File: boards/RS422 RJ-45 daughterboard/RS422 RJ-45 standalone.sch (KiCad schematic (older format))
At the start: 13 parts, among them J201 DB9, J202 DB9, U201 ISL83387E, U202 24AA014

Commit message: Done RS422/485 Daughterboard
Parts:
- removed J202: DB9, symbol DB9
- added J202: RJ45, symbol RJ45
- added P201: CONN_4, symbol CONN_4
- added SW201: DPDT, ~, symbol DPDT_SLIDE-SWITCH
- added U203: ISL8491E, ~, symbol ISL8491E
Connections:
- net labels removed: C_CTS, C_DSR, C_DTR, C_RTS, C_RX, C_TX
- wire segments 90 -> 112
- no-connect marks 4 -> 7
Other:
- moved on the sheet: D201, J201, R201, R203, U201, U202

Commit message: Update RS422 RJ-45 dboard to use RS232 adapter common block
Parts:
- removed C201, C202, C203, C204, C205, C206: 0.1u, ~, symbol CSMALL
- removed D201: LED, ~, symbol LED
- removed J201: DB9, symbol DB9
- removed R201: R, ~, symbol R
- removed U201: ISL83387E, ~, symbol ISL83387E
- added J201: RJ45, symbol RJ45
- added P202: CONN_4X2, symbol CONN_4X2
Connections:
- net labels removed: A_CTS, A_DSR, A_DTR, A_RTS, A_RX, A_TX, B_CTS, B_DSR, B_DTR, B_RTS, B_RX, B_TX
- wire segments 112 -> 72
- no-connect marks 7 -> 10
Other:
- moved on the sheet: J202, P201, SW201, U203

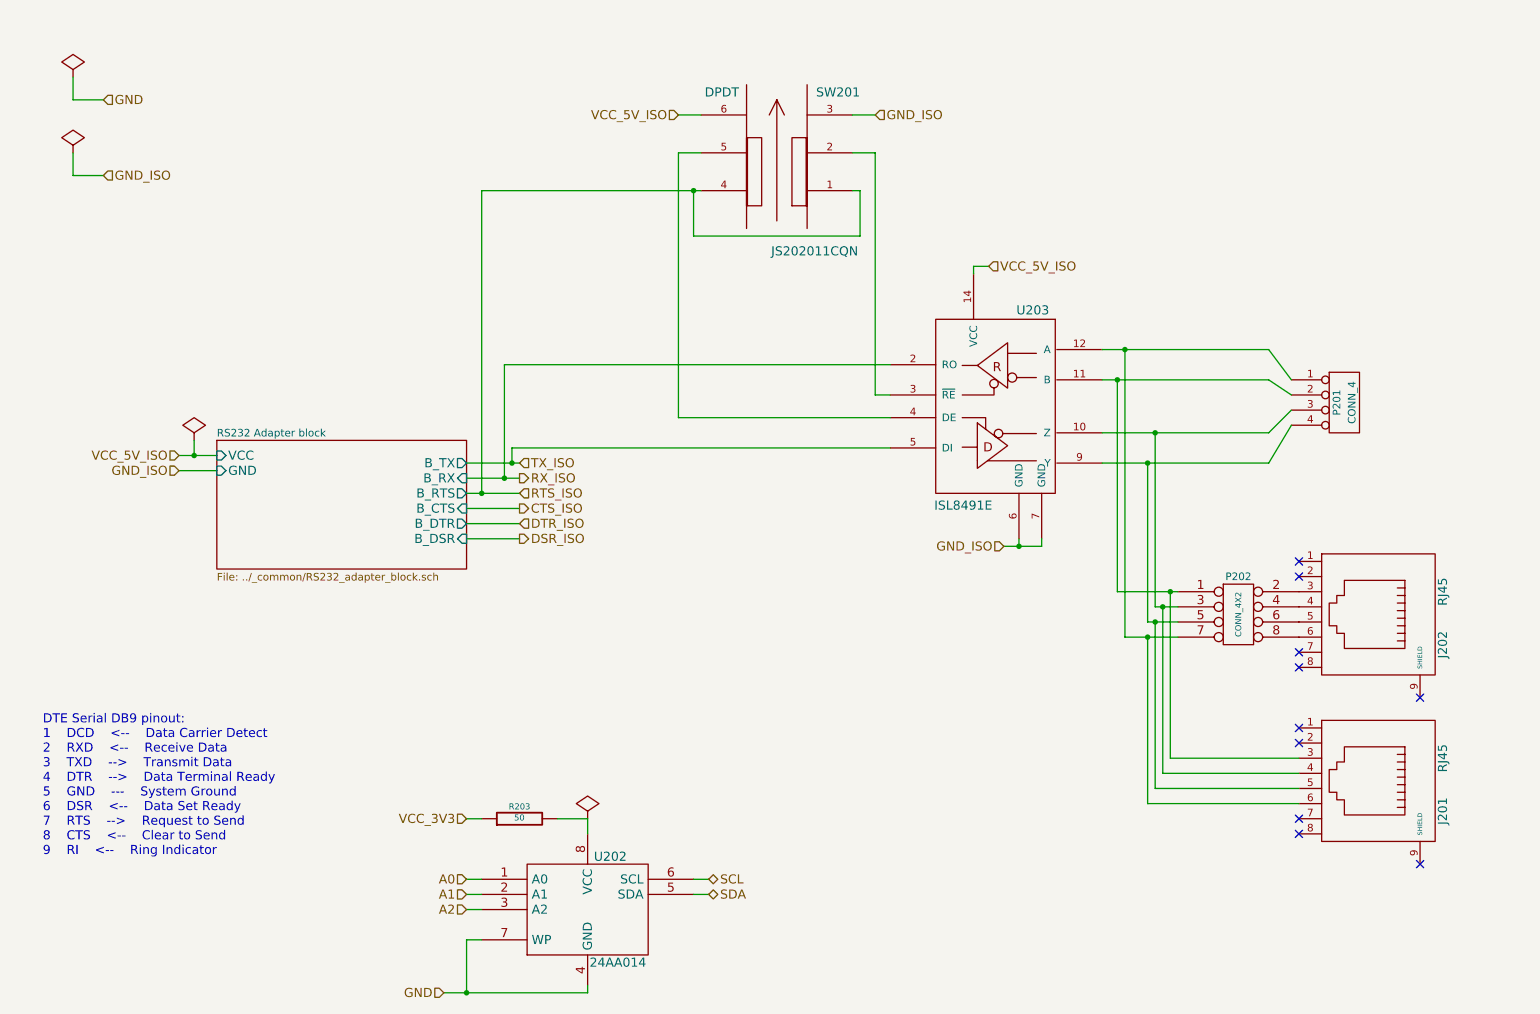
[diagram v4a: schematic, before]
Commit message: Updated RS232 adapter block to include DC jack, changed power pins to passive; Changed power pins on RS422 dboard sheet to passive
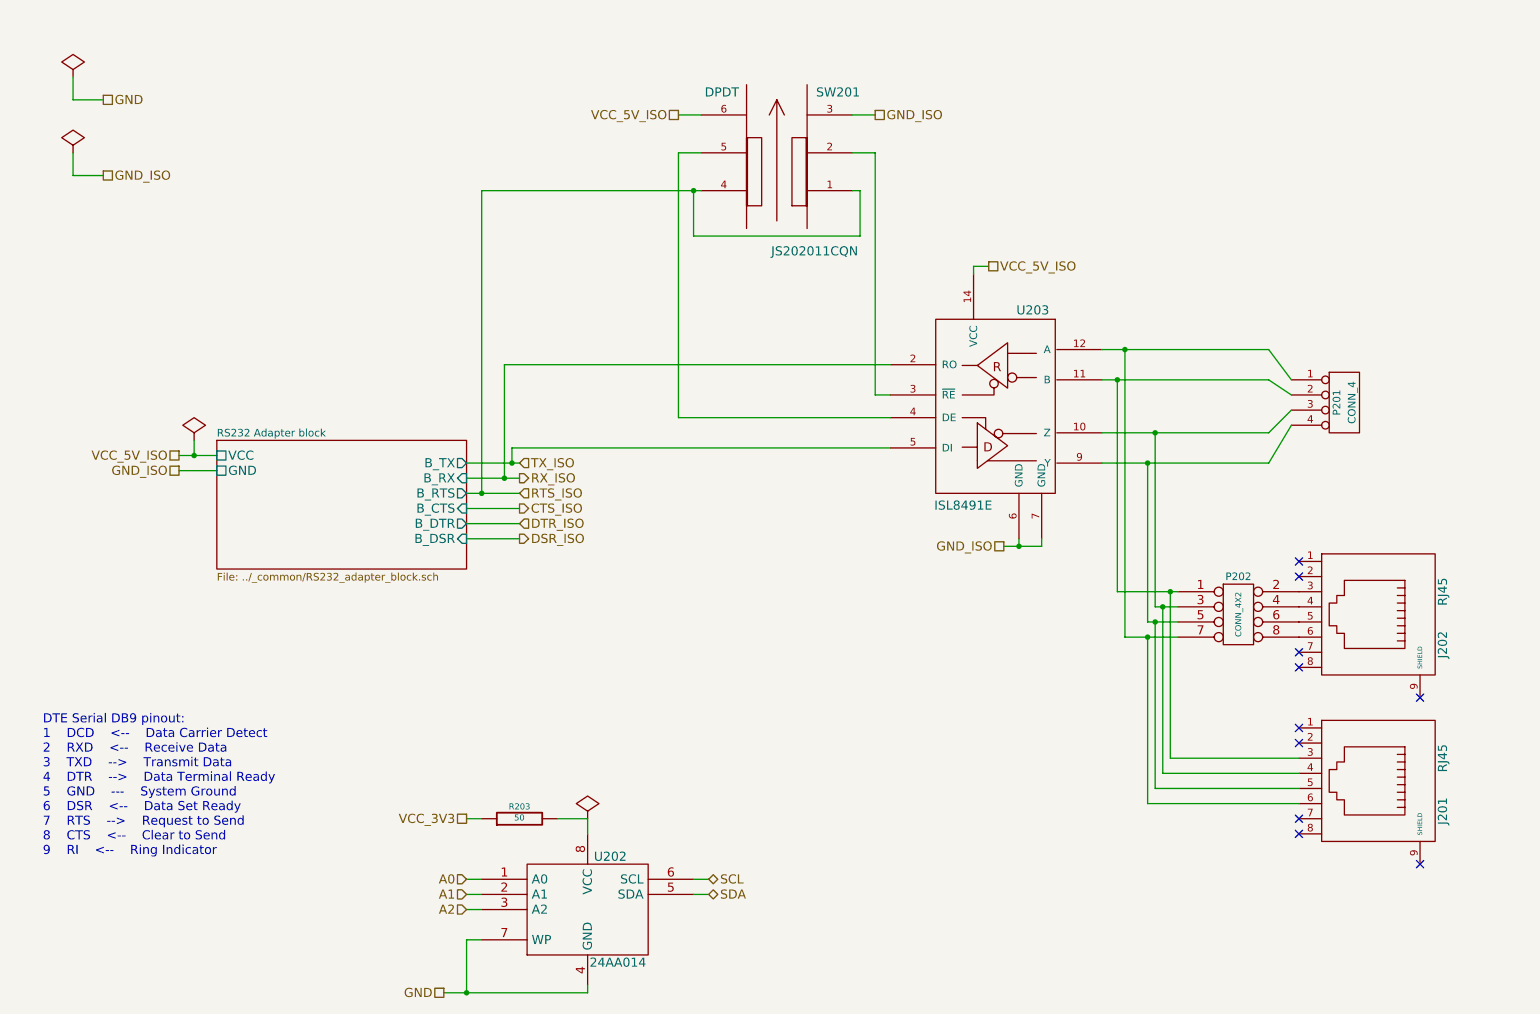
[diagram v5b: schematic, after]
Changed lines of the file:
@@
 Text HLabel 4200 4350 2    60   Output ~ 0
 DSR_ISO
-Text HLabel 3850 6200 0    60   Input ~ 0
+Text HLabel 3850 6200 0    60   UnSpc ~ 0
 VCC_3V3
-Text HLabel 3700 7350 0    60   Input ~ 0
+Text HLabel 3700 7350 0    60   UnSpc ~ 0
 GND
 Text HLabel 5450 6700 2    60   BiDi ~ 0
@@
 	1    0    0    -1
 $EndComp
-Text HLabel 1950 3800 0    60   Input ~ 0
+Text HLabel 1950 3800 0    60   UnSpc ~ 0
 VCC_5V_ISO
-Text HLabel 1950 3900 0    60   Input ~ 0
+Text HLabel 1950 3900 0    60   UnSpc ~ 0
 GND_ISO
 Text Notes 1050 6450 0    60   ~ 0
 DTE Serial DB9 pinout:\n1	DCD	<--	Data Carrier Detect\n2	RXD	<--	Receive Data\n3	TXD	-->	Transmit Data\n4	DTR	-->	Data Terminal Ready\n5	GND	---	System Ground\n6	DSR	<--	Data Set Ready\n7	RTS	-->	Request to Send\n8	CTS	<--	Clear to Send\n9	RI	<--	Ring Indicator
 $Comp
-L PWR_FLAG #FLG01
+L PWR_FLAG #FLG203
 U 1 1 53ABE834
 P 2050 3700
-F 0 "#FLG01" H 2050 3795 30  0001 C CNN
+F 0 "#FLG203" H 2050 3795 30  0001 C CNN
 F 1 "PWR_FLAG" H 2050 3880 30  0001 C CNN
 F 2 "" H 2050 3700 60  0000 C CNN
@@
 $EndComp
 $Comp
-L PWR_FLAG #FLG02
+L PWR_FLAG #FLG204
 U 1 1 53ABE907
 P 4650 6200
-F 0 "#FLG02" H 4650 6295 30  0001 C CNN
+F 0 "#FLG204" H 4650 6295 30  0001 C CNN
 F 1 "PWR_FLAG" H 4650 6380 30  0001 C CNN
 F 2 "" H 4650 6200 60  0000 C CNN
@@
 $EndComp
 $Comp
-L PWR_FLAG #FLG03
+L PWR_FLAG #FLG201
 U 1 1 53ABE910
 P 1250 1300
-F 0 "#FLG03" H 1250 1395 30  0001 C CNN
+F 0 "#FLG201" H 1250 1395 30  0001 C CNN
 F 1 "PWR_FLAG" H 1250 1480 30  0001 C CNN
 F 2 "" H 1250 1300 60  0000 C CNN
@@
 $EndComp
 $Comp
-L PWR_FLAG #FLG04
+L PWR_FLAG #FLG202
 U 1 1 53ABE916
 P 1250 1800
-F 0 "#FLG04" H 1250 1895 30  0001 C CNN
+F 0 "#FLG202" H 1250 1895 30  0001 C CNN
 F 1 "PWR_FLAG" H 1250 1980 30  0001 C CNN
 F 2 "" H 1250 1800 60  0000 C CNN
@@
 	1    0    0    -1
 $EndComp
-Text HLabel 1450 1450 2    60   Input ~ 0
+Text HLabel 1450 1450 2    60   UnSpc ~ 0
 GND
-Text HLabel 1450 1950 2    60   Input ~ 0
+Text HLabel 1450 1950 2    60   UnSpc ~ 0
 GND_ISO
 $Comp
@@
 	0    1    1    0
 $EndComp
-Text HLabel 7300 2550 2    60   Input ~ 0
+Text HLabel 7300 2550 2    60   UnSpc ~ 0
 VCC_5V_ISO
-Text HLabel 7400 4400 0    60   Input ~ 0
+Text HLabel 7400 4400 0    60   UnSpc ~ 0
 GND_ISO
 $Comp
@@
 	0    -1   -1   0
 $EndComp
-Text HLabel 5250 1550 0    60   Input ~ 0
+Text HLabel 5250 1550 0    60   UnSpc ~ 0
 VCC_5V_ISO
-Text HLabel 6550 1550 2    60   Input ~ 0
+Text HLabel 6550 1550 2    60   UnSpc ~ 0
 GND_ISO
 Wire Wire Line
@@
 F0 "RS232 Adapter block" 50
 F1 "../_common/RS232_adapter_block.sch" 50
-F2 "GND" I L 2200 3900 60
-F3 "VCC" I L 2200 3800 60
+F2 "GND" U L 2200 3900 60
+F3 "VCC" U L 2200 3800 60
 F4 "B_RX" I R 3850 3950 60
 F5 "B_TX" O R 3850 3850 60

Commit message: Added bypass capacitor to EEPROM in RS422 dboard
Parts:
- added C201: 0.1u, ~, symbol CSMALL
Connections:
- wire segments 72 -> 75
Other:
- note removed: "DTE Serial DB9 pinout:\n1 DCD <-- Data Carrier Detect\n2 RXD <-- Receive Data\n3 TXD --> Transmit Data\n4 DTR --> Data Terminal Ready\n5 GND --- System Ground\n6 DSR <-- Data Set Ready\n7 RTS --> Request to Send\n8 CTS <-- Clear to Send\n9 RI <-- Ring Indicator"
- moved on the sheet: R203
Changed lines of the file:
@@
 Sheet 2 3
 Title ""
-Date "2 jul 2014"
+Date "3 jul 2014"
 Rev ""
 Comp ""
@@
 Text HLabel 4200 4350 2    60   Output ~ 0
 DSR_ISO
-Text HLabel 3850 6200 0    60   UnSpc ~ 0
+Text HLabel 3350 6200 0    60   UnSpc ~ 0
 VCC_3V3
 Text HLabel 3700 7350 0    60   UnSpc ~ 0
@@
 Text HLabel 1950 3900 0    60   UnSpc ~ 0
 GND_ISO
-Text Notes 1050 6450 0    60   ~ 0
-DTE Serial DB9 pinout:\n1	DCD	<--	Data Carrier Detect\n2	RXD	<--	Receive Data\n3	TXD	-->	Transmit Data\n4	DTR	-->	Data Terminal Ready\n5	GND	---	System Ground\n6	DSR	<--	Data Set Ready\n7	RTS	-->	Request to Send\n8	CTS	<--	Clear to Send\n9	RI	<--	Ring Indicator
 $Comp
 L PWR_FLAG #FLG203
@@
 L R R203
 U 1 1 53ABAC25
-P 4200 6200
-F 0 "R203" V 4280 6200 40  0000 C CNN
-F 1 "50" V 4207 6201 40  0000 C CNN
-F 2 "~" V 4130 6200 30  0000 C CNN
-F 3 "~" H 4200 6200 30  0000 C CNN
-	1    4200 6200
+P 3700 6200
+F 0 "R203" V 3780 6200 40  0000 C CNN
+F 1 "50" V 3707 6201 40  0000 C CNN
+F 2 "~" V 3630 6200 30  0000 C CNN
+F 3 "~" H 3700 6200 30  0000 C CNN
+	1    3700 6200
 	0    -1   -1   0
 $EndComp
@@
 	5450 6700 5350 6700
 Wire Wire Line
-	4450 6200 4650 6200
+	3950 6200 4650 6200
 Wire Wire Line
 	4650 6200 4650 6300
@@
 	1250 1950 1450 1950
 Wire Wire Line
-	3950 6200 3850 6200
+	3450 6200 3350 6200
 Wire Wire Line
 	7300 2550 7200 2550
@@
 	8350 6100 8350 5000
 Connection ~ 8350 5000
+$Comp
+L CSMALL C201
+U 1 1 53B518F0
+P 4200 6000
+F 0 "C201" H 4225 6050 30  0000 L CNN
+F 1 "0.1u" H 4225 5950 30  0000 L CNN
+F 2 "~" H 4200 6000 60  0000 C CNN
+F 3 "~" H 4200 6000 60  0000 C CNN
+	1    4200 6000
+	1    0    0    -1
+$EndComp
+Wire Wire Line
+	4200 6100 4200 6200
+Connection ~ 4200 6200
+Wire Wire Line
+	4200 5900 4200 5800
+Wire Wire Line
+	4200 5800 3850 5800
+Text HLabel 3850 5800 0    60   UnSpc ~ 0
+GND
 $EndSCHEMATC

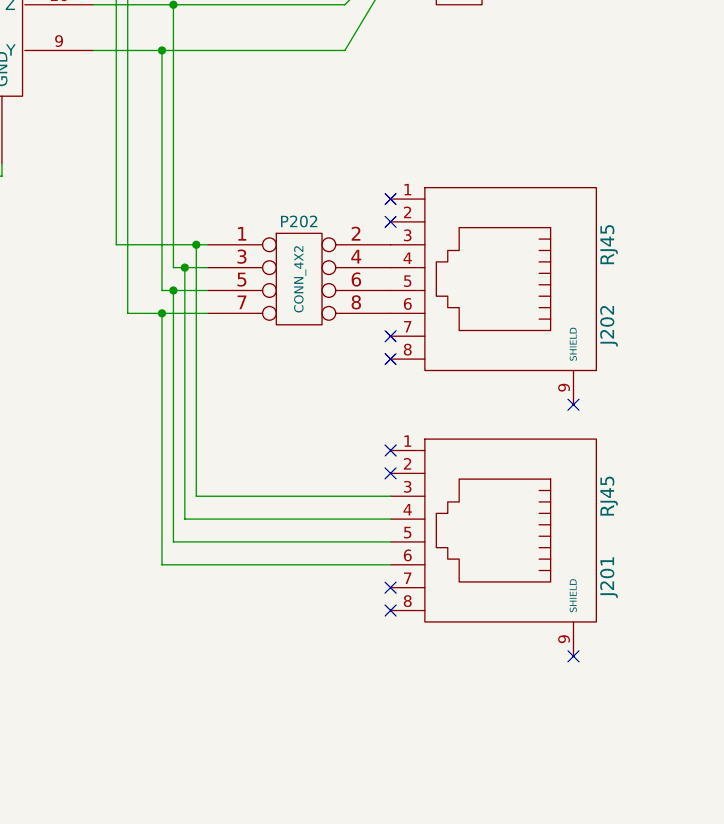
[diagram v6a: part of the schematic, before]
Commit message: Changed pinout conf headers in RS422 dboard and changed hierarchical pin types
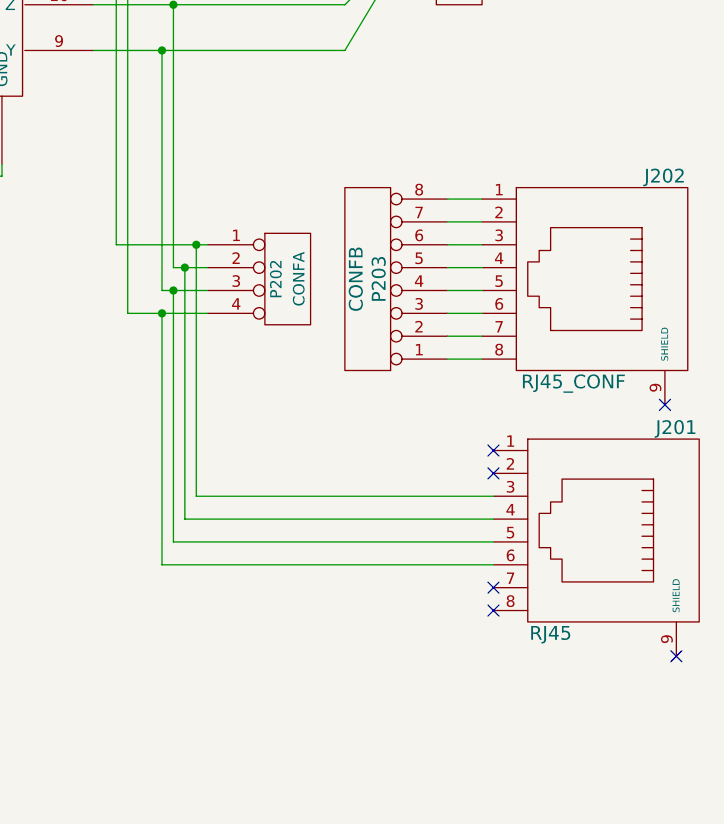
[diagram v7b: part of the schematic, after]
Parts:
- removed P202: CONN_4X2, symbol CONN_4X2
- added P202: CONFA, symbol CONN_4
- added P203: CONFB, symbol CONN_8
- J202: value RJ45 -> RJ45_CONF
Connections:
- wire segments 75 -> 83
- no-connect marks 10 -> 6
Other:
- moved on the sheet: J201, J202
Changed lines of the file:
@@
 GND_ISO
 $Comp
-L PWR_FLAG #FLG203
+L PWR_FLAG #FLG01
 U 1 1 53ABE834
 P 2050 3700
-F 0 "#FLG203" H 2050 3795 30  0001 C CNN
+F 0 "#FLG01" H 2050 3795 30  0001 C CNN
 F 1 "PWR_FLAG" H 2050 3880 30  0001 C CNN
 F 2 "" H 2050 3700 60  0000 C CNN
@@
 $EndComp
 $Comp
-L PWR_FLAG #FLG204
+L PWR_FLAG #FLG02
 U 1 1 53ABE907
 P 4650 6200
-F 0 "#FLG204" H 4650 6295 30  0001 C CNN
+F 0 "#FLG02" H 4650 6295 30  0001 C CNN
 F 1 "PWR_FLAG" H 4650 6380 30  0001 C CNN
 F 2 "" H 4650 6200 60  0000 C CNN
@@
 $EndComp
 $Comp
-L PWR_FLAG #FLG201
+L PWR_FLAG #FLG03
 U 1 1 53ABE910
 P 1250 1300
-F 0 "#FLG201" H 1250 1395 30  0001 C CNN
+F 0 "#FLG03" H 1250 1395 30  0001 C CNN
 F 1 "PWR_FLAG" H 1250 1480 30  0001 C CNN
 F 2 "" H 1250 1300 60  0000 C CNN
@@
 $EndComp
 $Comp
-L PWR_FLAG #FLG202
+L PWR_FLAG #FLG04
 U 1 1 53ABE916
 P 1250 1800
-F 0 "#FLG202" H 1250 1895 30  0001 C CNN
+F 0 "#FLG04" H 1250 1895 30  0001 C CNN
 F 1 "PWR_FLAG" H 1250 1980 30  0001 C CNN
 F 2 "" H 1250 1800 60  0000 C CNN
@@
 L RJ45 J202
 U 1 1 53AFC1B5
-P 9800 4850
-F 0 "J202" H 10000 5350 60  0000 C CNN
-F 1 "RJ45" H 9650 5350 60  0000 C CNN
-F 2 "" H 9800 4850 60  0000 C CNN
-F 3 "" H 9800 4850 60  0000 C CNN
-	1    9800 4850
+P 10200 4850
+F 0 "J202" V 9750 5200 60  0000 C CNN
+F 1 "RJ45_CONF" V 10650 4800 60  0000 C CNN
+F 2 "" H 10200 4850 60  0000 C CNN
+F 3 "" H 10200 4850 60  0000 C CNN
+	1    10200 4850
 	0    1    1    0
 $EndComp
@@
 	8350 4900 8550 4900
 Connection ~ 8350 3850
-NoConn ~ 9350 4500
-NoConn ~ 9350 4600
-NoConn ~ 9350 5100
-NoConn ~ 9350 5200
-NoConn ~ 10150 5400
-$Comp
-L CONN_4X2 P202
-U 1 1 53B0C6CE
-P 8950 4850
-F 0 "P202" H 8950 5100 50  0000 C CNN
-F 1 "CONN_4X2" V 8950 4850 40  0000 C CNN
-F 2 "" H 8950 4850 60  0000 C CNN
-F 3 "" H 8950 4850 60  0000 C CNN
-	1    8950 4850
-	1    0    0    -1
-$EndComp
+NoConn ~ 10550 5400
 $Sheet
 S 2200 3700 1650 850
@@
 L RJ45 J201
 U 1 1 53B148F5
-P 9800 5950
-F 0 "J201" H 10000 6450 60  0000 C CNN
-F 1 "RJ45" H 9650 6450 60  0000 C CNN
-F 2 "" H 9800 5950 60  0000 C CNN
-F 3 "" H 9800 5950 60  0000 C CNN
-	1    9800 5950
+P 10250 5950
+F 0 "J201" V 9800 6300 60  0000 C CNN
+F 1 "RJ45" V 10700 5750 60  0000 C CNN
+F 2 "" H 10250 5950 60  0000 C CNN
+F 3 "" H 10250 5950 60  0000 C CNN
+	1    10250 5950
 	0    1    1    0
 $EndComp
-NoConn ~ 9350 5600
-NoConn ~ 9350 5700
-NoConn ~ 9350 6200
-NoConn ~ 9350 6300
-NoConn ~ 10150 6500
-Wire Wire Line
-	9350 5800 8500 5800
+NoConn ~ 9800 5600
+NoConn ~ 9800 5700
+NoConn ~ 9800 6200
+NoConn ~ 9800 6300
+NoConn ~ 10600 6500
+Wire Wire Line
+	9800 5800 8500 5800
 Wire Wire Line
 	8500 5800 8500 4700
 Connection ~ 8500 4700
 Wire Wire Line
-	9350 5900 8450 5900
+	9800 5900 8450 5900
 Wire Wire Line
 	8450 5900 8450 4800
 Connection ~ 8450 4800
 Wire Wire Line
-	9350 6000 8400 6000
+	9800 6000 8400 6000
 Wire Wire Line
 	8400 6000 8400 4900
 Connection ~ 8400 4900
 Wire Wire Line
-	9350 6100 8350 6100
+	9800 6100 8350 6100
 Wire Wire Line
 	8350 6100 8350 5000
@@
 Text HLabel 3850 5800 0    60   UnSpc ~ 0
 GND
+$Comp
+L CONN_4 P202
+U 1 1 53B55649
+P 8900 4850
+F 0 "P202" V 8850 4850 50  0000 C CNN
+F 1 "CONFA" V 8950 4850 50  0000 C CNN
+F 2 "" H 8900 4850 60  0000 C CNN
+F 3 "" H 8900 4850 60  0000 C CNN
+	1    8900 4850
+	1    0    0    -1
+$EndComp
+$Comp
+L CONN_8 P203
+U 1 1 53B55658
+P 9250 4850
+F 0 "P203" V 9200 4850 60  0000 C CNN
+F 1 "CONFB" V 9300 4850 60  0000 C CNN
+F 2 "" H 9250 4850 60  0000 C CNN
+F 3 "" H 9250 4850 60  0000 C CNN
+	1    9250 4850
+	-1   0    0    1
+$EndComp
+Wire Wire Line
+	9600 4500 9750 4500
+Wire Wire Line
+	9750 4600 9600 4600
+Wire Wire Line
+	9750 4700 9600 4700
+Wire Wire Line
+	9600 4800 9750 4800
+Wire Wire Line
+	9750 4900 9600 4900
+Wire Wire Line
+	9600 5000 9750 5000
+Wire Wire Line
+	9750 5100 9600 5100
+Wire Wire Line
+	9600 5200 9750 5200
 $EndSCHEMATC
